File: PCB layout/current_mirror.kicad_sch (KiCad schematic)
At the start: 21 parts, among them J1 12V INPUT, Q1 2N3904, Q2 2N3904

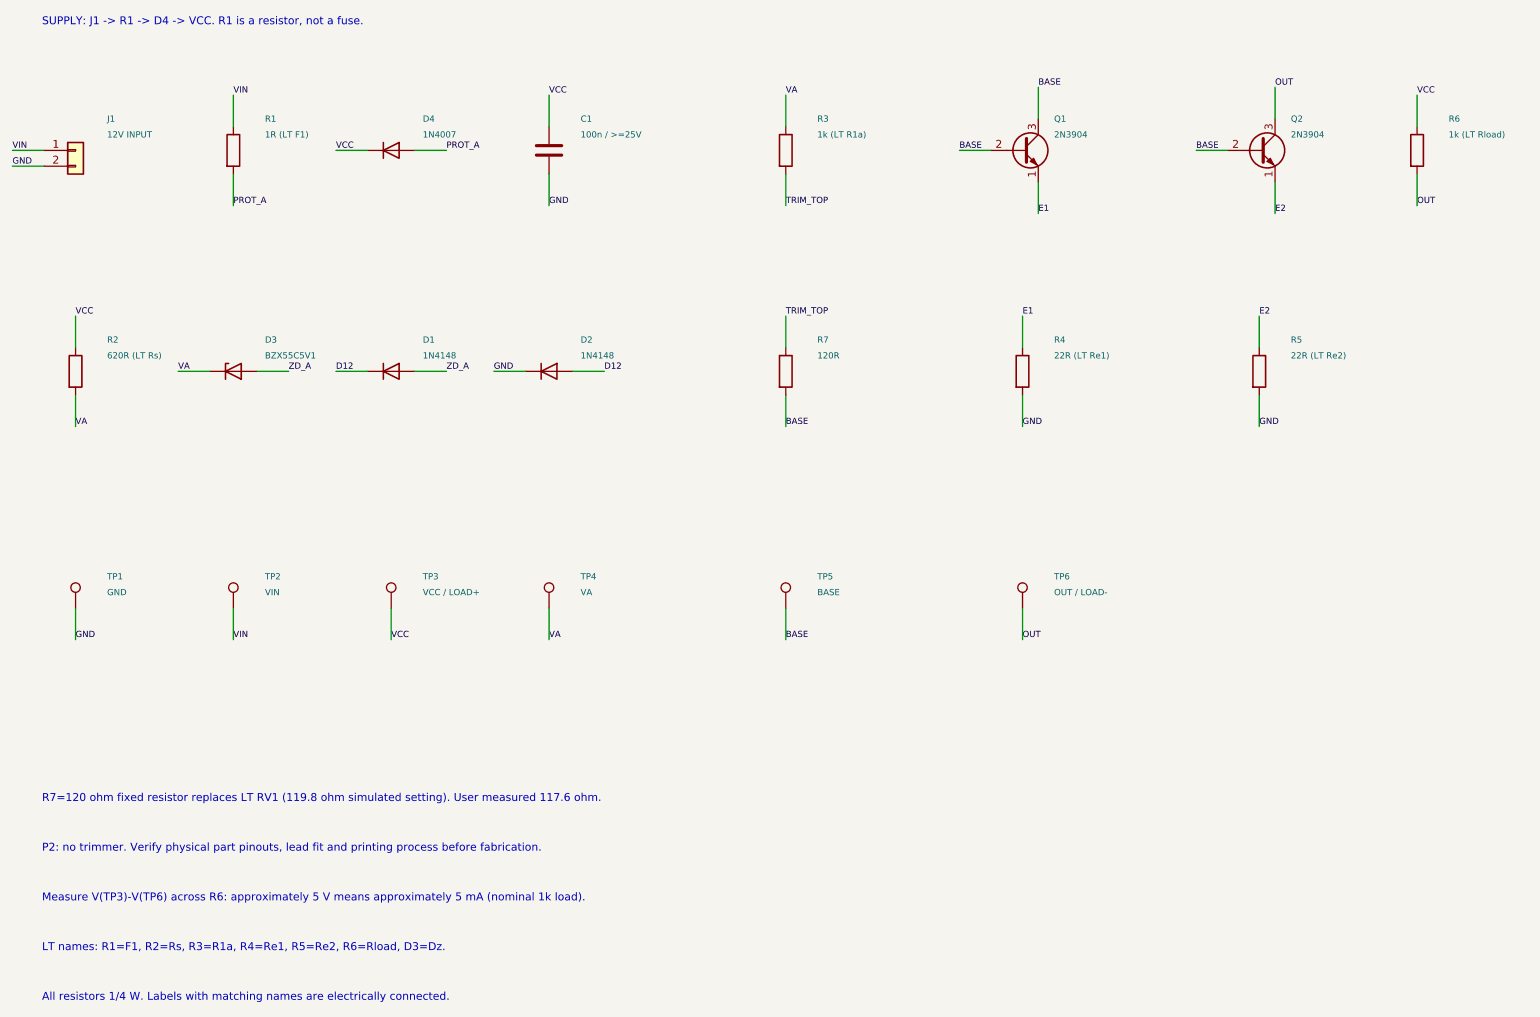
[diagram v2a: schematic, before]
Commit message: Sync PCB values with revised LTspice schematic and validate P3
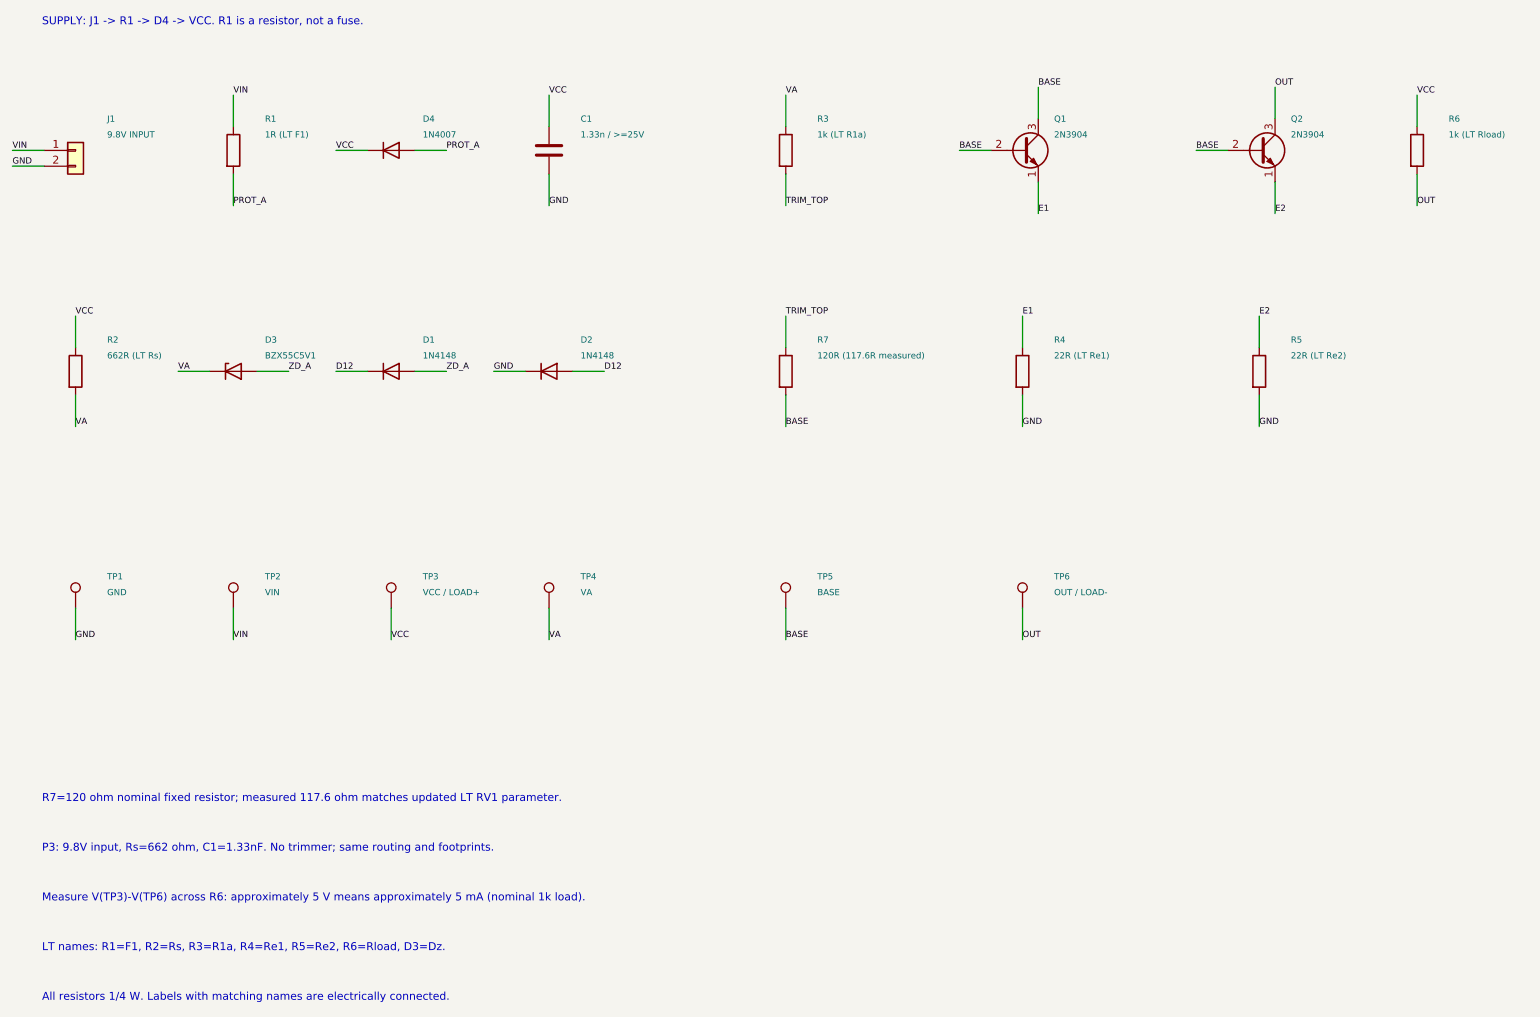
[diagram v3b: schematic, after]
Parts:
- C1: value 100n / >=25V -> 1.33n / >=25V
- J1: value 12V INPUT -> 9.8V INPUT
- R2: value 620R (LT Rs) -> 662R (LT Rs)
- R7: value 120R -> 120R (117.6R measured)
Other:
- note added: "P3: 9.8V input, Rs=662 ohm, C1=1.33nF. No trimmer; same routing and footprints."
- note added: "R7=120 ohm nominal fixed resistor; measured 117.6 ohm matches updated LT RV1 parameter."
- note removed: "P2: no trimmer. Verify physical part pinouts, lead fit and printing process before fabrication."
- note removed: "R7=120 ohm fixed resistor replaces LT RV1 (119.8 ohm simulated setting). User measured 117.6 ohm."
- title: 5 mA diode-compensated current mirror -> Diode-compensated current mirror
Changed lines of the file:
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@@
 (kicad_sch (version 20250114) (generator "pcb_layout_script") (paper "A4")
-(title_block (title "5 mA diode-compensated current mirror") (rev "P2 - FIXED 120R") (comment 1 "LTspice topology; RV1 replaced by fixed R7=120R at user request"))
+(title_block (title "Diode-compensated current mirror") (rev "P3 - SOURCE VALUES SYNC") (comment 1 "9.8V input; Rs=662R; C1=1.33nF; fixed R7=120R nominal, 117.6R measured"))
 (symbol (lib_id "Connector_Generic:Conn_01x02") (at 25.4 40.64 0) (unit 1) (in_bom yes) (on_board yes) (dnp no)
 (property "Reference" "J1" (at 30.479999999999997 35.56 0) (effects (font (size 1.0 1.0)) (justify left) ))
-(property "Value" "12V INPUT" (at 30.479999999999997 38.1 0) (effects (font (size 1.0 1.0)) (justify left) ))
+(property "Value" "9.8V INPUT" (at 30.479999999999997 38.1 0) (effects (font (size 1.0 1.0)) (justify left) ))
 (property "Footprint" "Project:J1_ETCH" (at 25.4 40.64 0) (effects (font (size 1.0 1.0)) (justify left) (hide yes)))
 (pin "1")
@@
 (symbol (lib_id "Device:C") (at 101.6 40.64 0) (unit 1) (in_bom yes) (on_board yes) (dnp no)
 (property "Reference" "C1" (at 106.67999999999999 35.56 0) (effects (font (size 1.0 1.0)) (justify left) ))
-(property "Value" "100n / >=25V" (at 106.67999999999999 38.1 0) (effects (font (size 1.0 1.0)) (justify left) ))
+(property "Value" "1.33n / >=25V" (at 106.67999999999999 38.1 0) (effects (font (size 1.0 1.0)) (justify left) ))
 (property "Footprint" "Project:C1_ETCH" (at 101.6 40.64 0) (effects (font (size 1.0 1.0)) (justify left) (hide yes)))
 (pin "1")
@@
 (symbol (lib_id "Device:R") (at 25.4 76.2 0) (unit 1) (in_bom yes) (on_board yes) (dnp no)
 (property "Reference" "R2" (at 30.479999999999997 71.12 0) (effects (font (size 1.0 1.0)) (justify left) ))
-(property "Value" "620R (LT Rs)" (at 30.479999999999997 73.66 0) (effects (font (size 1.0 1.0)) (justify left) ))
+(property "Value" "662R (LT Rs)" (at 30.479999999999997 73.66 0) (effects (font (size 1.0 1.0)) (justify left) ))
 (property "Footprint" "Project:R2_ETCH" (at 25.4 76.2 0) (effects (font (size 1.0 1.0)) (justify left) (hide yes)))
 (pin "1")
@@
 (symbol (lib_id "Device:R") (at 139.7 76.2 0) (unit 1) (in_bom yes) (on_board yes) (dnp no)
 (property "Reference" "R7" (at 144.78 71.12 0) (effects (font (size 1.0 1.0)) (justify left) ))
-(property "Value" "120R" (at 144.78 73.66 0) (effects (font (size 1.0 1.0)) (justify left) ))
+(property "Value" "120R (117.6R measured)" (at 144.78 73.66 0) (effects (font (size 1.0 1.0)) (justify left) ))
 (property "Footprint" "Project:R7_ETCH" (at 139.7 76.2 0) (effects (font (size 1.0 1.0)) (justify left) (hide yes)))
 (pin "1")
@@
 (label "OUT" (at 177.8 119.38 0) (effects (font (size 1.0 1.0)) (justify left bottom)))
 (text "SUPPLY: J1 -> R1 -> D4 -> VCC. R1 is a resistor, not a fuse." (at 20 20 0) (effects (font (size 1.27 1.27)) (justify left)))
-(text "R7=120 ohm fixed resistor replaces LT RV1 (119.8 ohm simulated setting). User measured 117.6 ohm." (at 20 145 0) (effects (font (size 1.27 1.27)) (justify left)))
-(text "P2: no trimmer. Verify physical part pinouts, lead fit and printing process before fabrication." (at 20 153 0) (effects (font (size 1.27 1.27)) (justify left)))
+(text "R7=120 ohm nominal fixed resistor; measured 117.6 ohm matches updated LT RV1 parameter." (at 20 145 0) (effects (font (size 1.27 1.27)) (justify left)))
+(text "P3: 9.8V input, Rs=662 ohm, C1=1.33nF. No trimmer; same routing and footprints." (at 20 153 0) (effects (font (size 1.27 1.27)) (justify left)))
 (text "Measure V(TP3)-V(TP6) across R6: approximately 5 V means approximately 5 mA (nominal 1k load)." (at 20 161 0) (effects (font (size 1.27 1.27)) (justify left)))
 (text "LT names: R1=F1, R2=Rs, R3=R1a, R4=Re1, R5=Re2, R6=Rload, D3=Dz." (at 20 169 0) (effects (font (size 1.27 1.27)) (justify left)))
